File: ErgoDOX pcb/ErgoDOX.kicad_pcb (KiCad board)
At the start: 2 copper layers, 182.8 x 158.9 mm, 72 parts, among them J1 USB, J2 3.5mm, J3 JMP, J4 JMP, SW0:10 SW0:3, SW0:11 SW0:2, SW0:12 SW0:1, SW0:7 SW0:6, SW0:8 SW0:5, SW0:9 SW0:4, SW1:10 SW1:3, SW1:11 SW1:2, SW1:12 SW1:1, SW1:13 SW1:0, SW1:9 SW1:4, SW2:10 SW2:3, SW2:11 SW2:2, SW2:12 SW2:1, SW2:13 SW2:0, SW2:7 SW2:6, SW2:8 SW2:5, SW2:9 SW2:4, SW3:10 SW3:3, SW3:11 SW3:2, SW3:12 SW3:1, SW3:13 SW3:0, SW3:8 SW3:5, SW3:9 SW3:4, SW4:10 SW4:3, SW4:11 SW4:2, SW4:12 SW4:1, SW4:13 SW4:0, SW4:7 SW4:6, SW4:8 SW4:5, SW4:9 SW4:4, SW5:10 SW5:3, SW5:11 SW5:2, SW5:12 SW5:1, SW5:13 SW5:0, SW5:7 SW5:6, SW5:8 SW5:5, SW5:9 SW5:4, U1 TEENSY2.0, U2 MCP23018

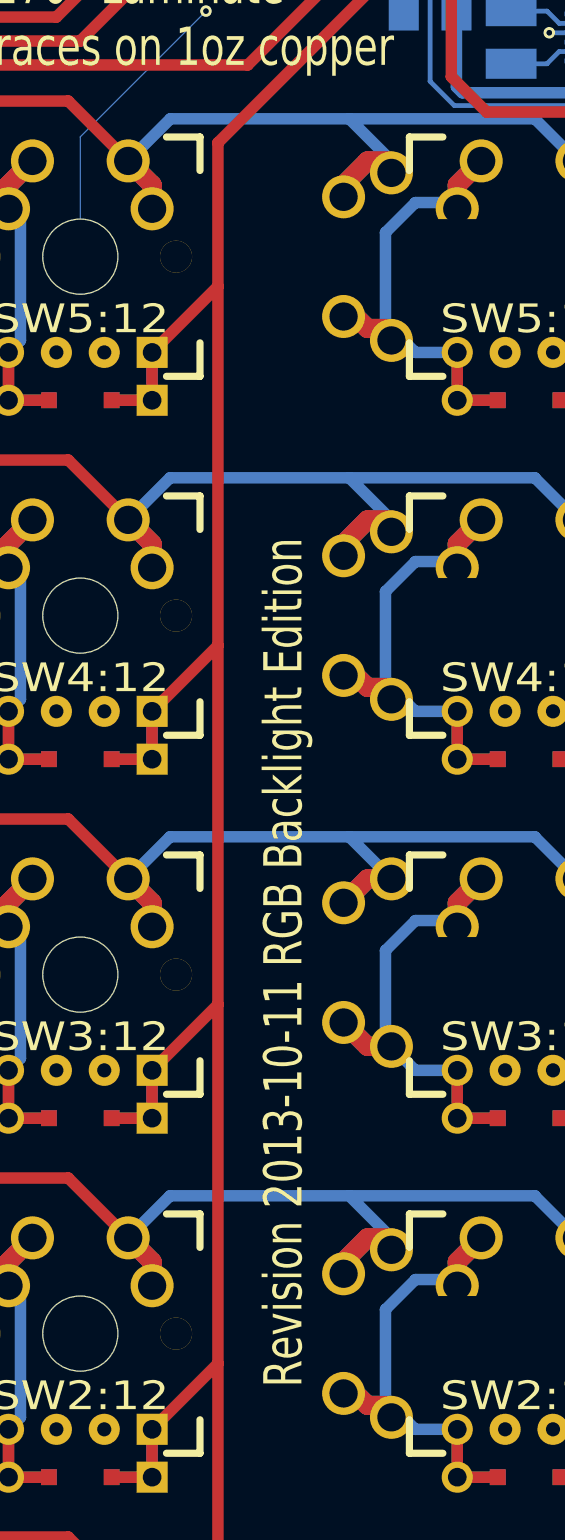
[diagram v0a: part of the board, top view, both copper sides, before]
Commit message: Fixed tracks around secondary outer most column
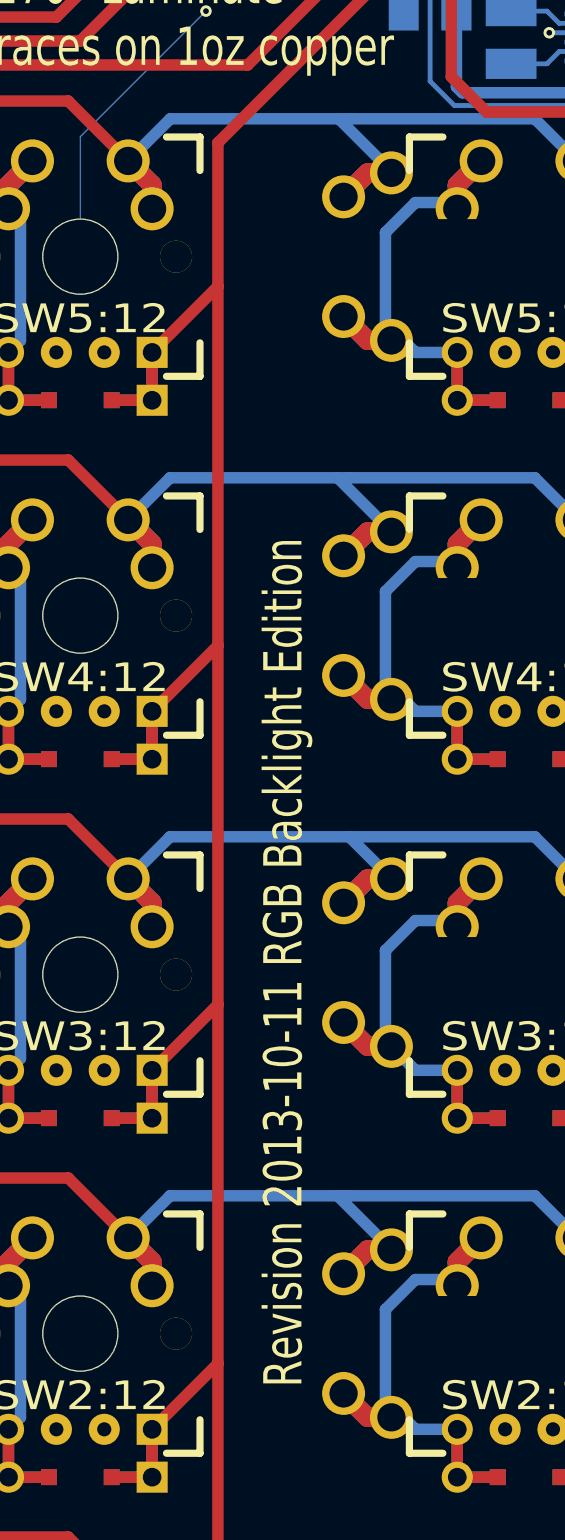
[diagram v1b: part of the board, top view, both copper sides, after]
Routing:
- net /ROW4: track 259.2 -> 260.1 mm
- net /ROW2: track 297.1 -> 298.0 mm
- net /ROW5: track 226.9 -> 227.7 mm

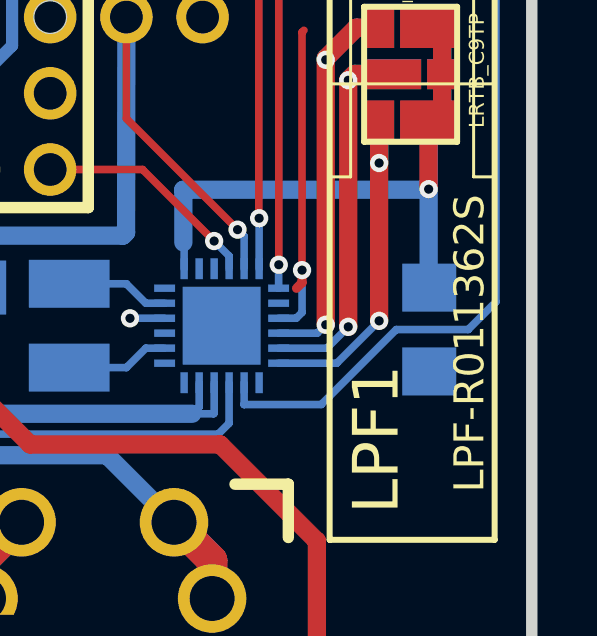
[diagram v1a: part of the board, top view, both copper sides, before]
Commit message: Allow output cap for led driver on either side.
Otherwise it might interfere with light tube.

Also fixed ground connection for all caps.
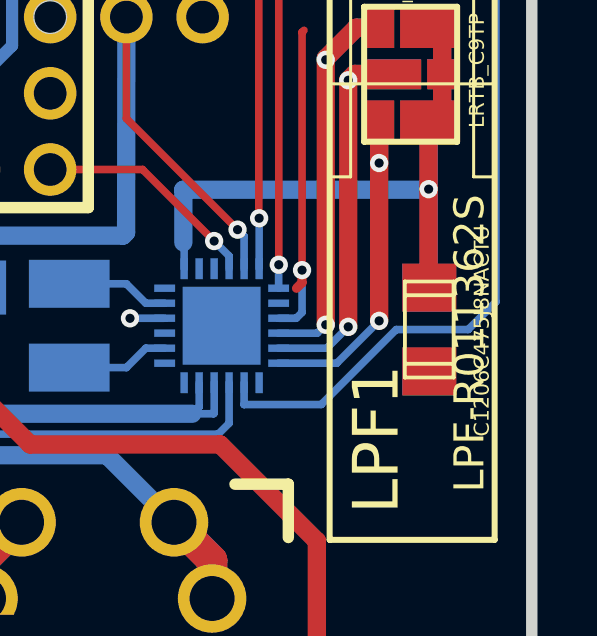
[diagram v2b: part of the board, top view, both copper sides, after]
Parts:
- added C1206C475J8NACTU: COUT1, C1206C475J8NACTU, F.Cu at (202.5, 55.5)
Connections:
- CIN1 pad 1: (no net) -> GND
- COUT1 pad 1: (no net) -> GND
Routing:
- net /V_OUT_C_CATHODE: track 25.8 -> 29.1 mm
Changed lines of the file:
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@@
 (kicad_pcb (version 3) (host pcbnew "(2013-07-07 BZR 4022)-stable")
   (general
-    (links 508)
-    (no_connects 3)
+    (links 511)
+    (no_connects 4)
     (area 22.890479 28.163519 259.962628 189.542421)
     (thickness 1.6002)
     (drawings 39)
-    (tracks 1306)
+    (tracks 1308)
     (zones 0)
-    (modules 72)
+    (modules 73)
     (nets 75)
   )
@@
     (mod_text_size 1.524 1.524)
     (mod_text_width 0.3048)
-    (pad_size 1.651 1.651)
-    (pad_drill 0.75)
+    (pad_size 1.6002 1.8034)
+    (pad_drill 0)
     (pad_to_mask_clearance 0.2032)
     (aux_axis_origin 0 0)
@@
     (pad 1 smd rect (at 1.397 0 180) (size 1.6002 1.8034)
       (layers Back B.Paste B.Mask)
+      (net 28 GND)
     )
     (pad 2 smd rect (at -1.397 0 180) (size 1.6002 1.8034)
@@
     (pad 1 smd rect (at 1.397 0 270) (size 1.6002 1.8034)
       (layers Back B.Paste B.Mask)
+      (net 28 GND)
     )
     (pad 2 smd rect (at -1.397 0 270) (size 1.6002 1.8034)
@@
     )
   )
+  (module C1206C475J8NACTU (layer Front)
+    (at 202.5015 55.499 270)
+    (descr "SMT capacitor, 1206")
+    (fp_text reference C1206C475J8NACTU (at 0.05 -1.75 270) (layer F.SilkS)
+      (effects (font (size 0.50038 0.50038) (thickness 0.11938)))
+    )
+    (fp_text value COUT1 (at 0.05 1.65 270) (layer F.SilkS) hide
+      (effects (font (size 0.50038 0.50038) (thickness 0.11938)))
+    )
+    (fp_line (start 1.143 0.8128) (end 1.143 -0.8128) (layer F.SilkS) (width 0.127))
+    (fp_line (start -1.143 -0.8128) (end -1.143 0.8128) (layer F.SilkS) (width 0.127))
+    (fp_line (start -1.6002 -0.8128) (end -1.6002 0.8128) (layer F.SilkS) (width 0.127))
+    (fp_line (start -1.6002 0.8128) (end 1.6002 0.8128) (layer F.SilkS) (width 0.127))
+    (fp_line (start 1.6002 0.8128) (end 1.6002 -0.8128) (layer F.SilkS) (width 0.127))
+    (fp_line (start 1.6002 -0.8128) (end -1.6002 -0.8128) (layer F.SilkS) (width 0.127))
+    (pad 1 smd rect (at 1.397 0 270) (size 1.6002 1.8034)
+      (layers Front F.Paste F.Mask)
+      (net 28 GND)
+    )
+    (pad 2 smd rect (at -1.397 0 270) (size 1.6002 1.8034)
+      (layers Front F.Paste F.Mask)
+    )
+    (model smd/capacitors/c_1206.wrl
+      (at (xyz 0 0 0))
+      (scale (xyz 1 1 1))
+      (rotate (xyz 0 0 0))
+    )
+  )
   (gr_text "Revision 2013-10-11 RGB Backlight Edition" (at 178.435 127 90) (layer F.SilkS)
     (effects (font (size 2.032 1.524) (thickness 0.3048)) (justify left))
@@
   (segment (start 171.45 139.39266) (end 171.45 140.66266) (width 1.016) (layer Back) (net 18))
   (segment (start 62.75832 145.59788) (end 64.9097 139.69238) (width 0.6096) (layer Back) (net 18))
-  (segment (start 184.15 119.70766) (end 184.15 119.6975) (width 0.6096) (layer Back) (net 19) (status C00000))
-  (segment (start 184.15 119.6975) (end 181.2925 116.84) (width 0.6096) (layer Back) (net 19) (status 400000))
+  (segment (start 184.15 119.70766) (end 184.15 119.6975) (width 0.6096) (layer Back) (net 19))
+  (segment (start 184.15 119.6975) (end 181.2925 116.84) (width 0.6096) (layer Back) (net 19))
   (segment (start 184.15 119.70766) (end 182.88 119.70766) (width 1.016) (layer Back) (net 19))
   (segment (start 182.88 119.70766) (end 181.61 120.97766) (width 1.016) (layer Back) (net 19))
@@
   (segment (start 188.595 46.0375) (end 186.3725 48.26) (width 0.4064) (layer Back) (net 26))
   (segment (start 176.2125 46.6725) (end 160.9725 46.6725) (width 0.4064) (layer Front) (net 26))
+  (segment (start 202.48 50.82) (end 202.48 54.0805) (width 0.6096) (layer Front) (net 27) (status 800000))
+  (segment (start 202.48 54.0805) (end 202.5015 54.102) (width 0.6096) (layer Front) (net 27) (status C00000))
   (segment (start 202.48 50.82) (end 202.48 54.083) (width 0.6096) (layer Back) (net 27))
   (segment (start 194.303 50.84) (end 202.46 50.84) (width 0.6096) (layer Back) (net 27))

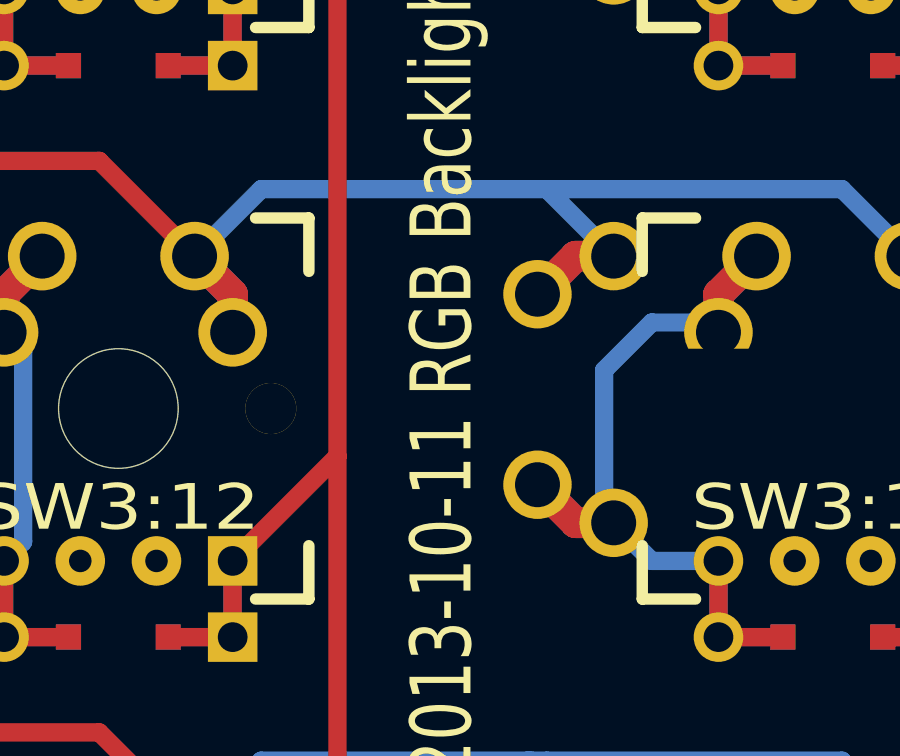
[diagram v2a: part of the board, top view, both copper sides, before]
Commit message: Fixed last switch secondary switch pos.
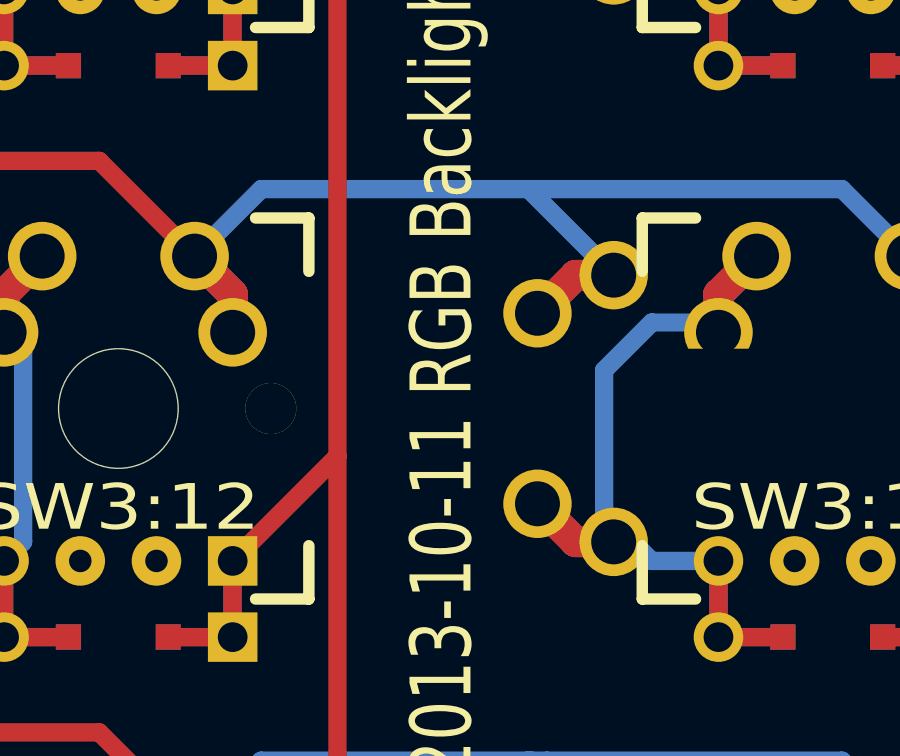
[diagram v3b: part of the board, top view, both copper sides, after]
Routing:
- net /ROW3: track 240.5 -> 241.4 mm

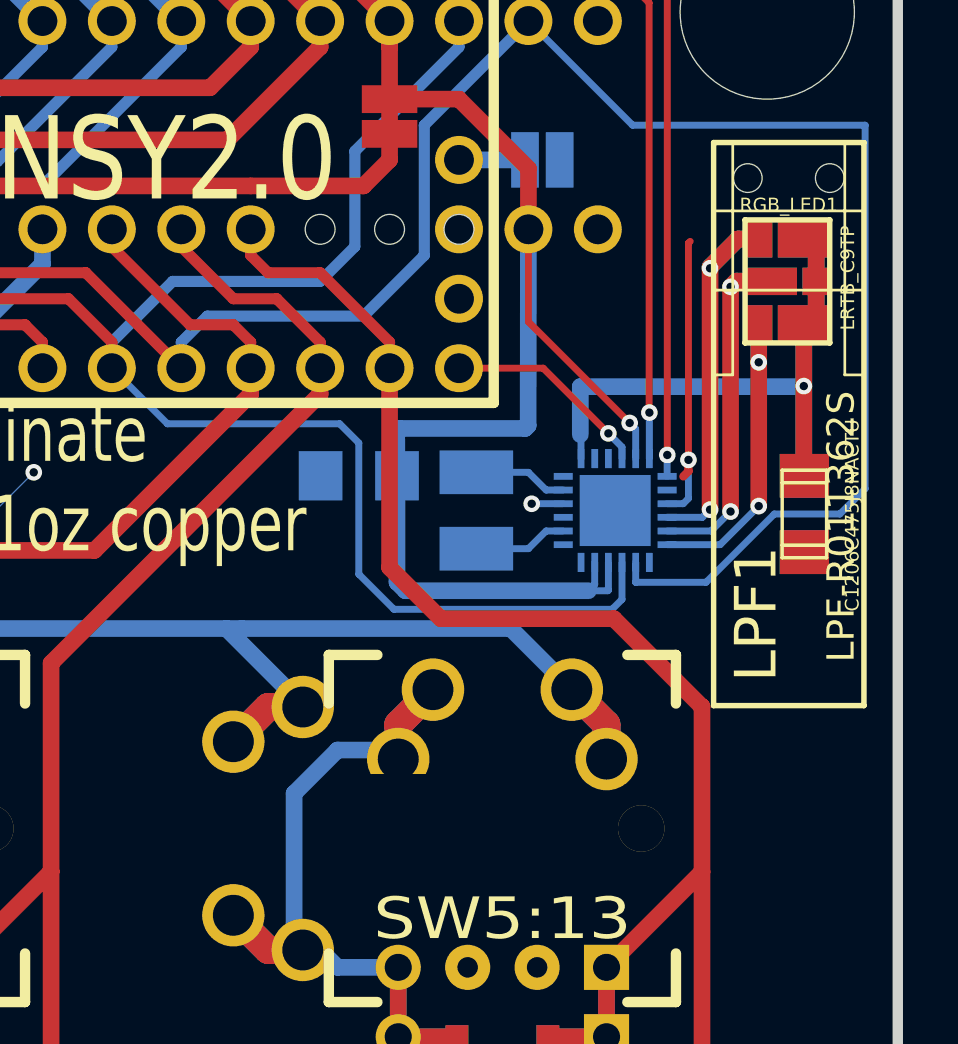
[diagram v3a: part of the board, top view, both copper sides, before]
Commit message: Allow dual side caps and inductor
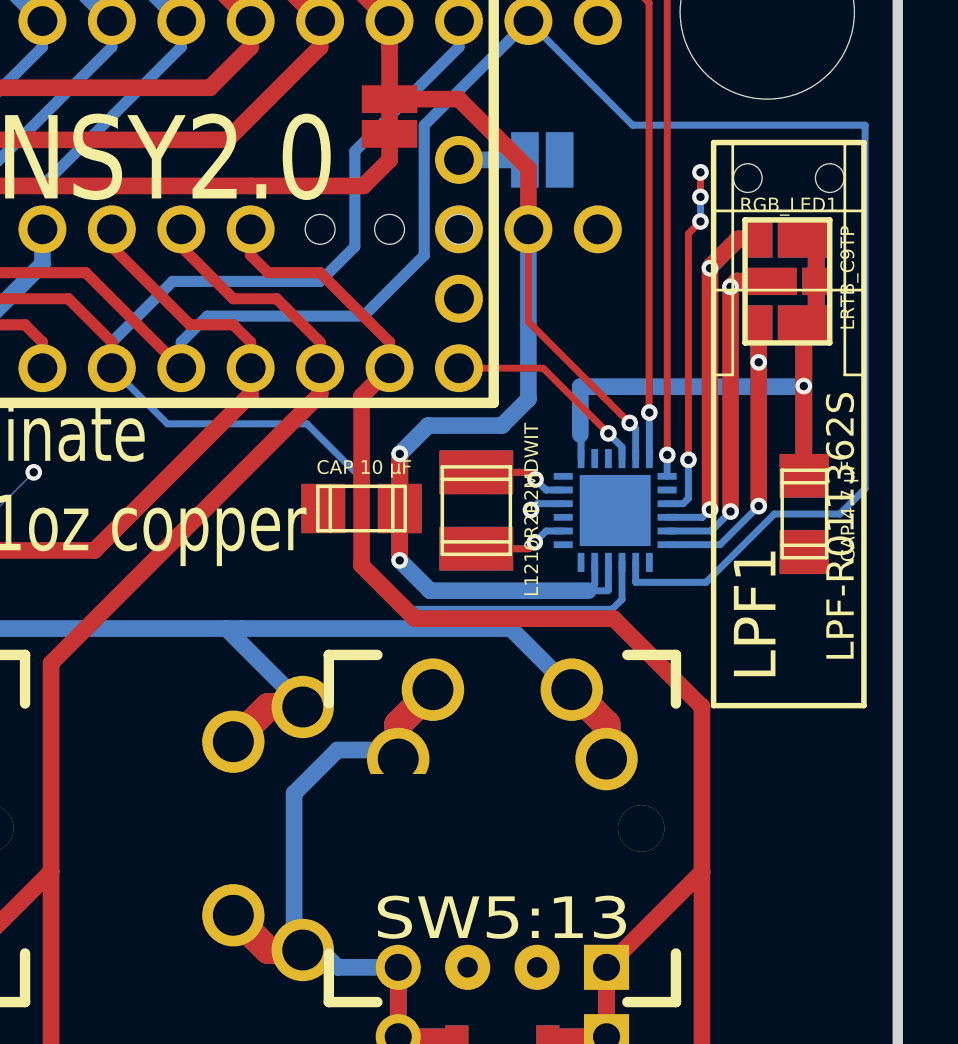
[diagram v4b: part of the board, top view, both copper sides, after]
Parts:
- added CAP 10 µF: CIN1, C1206C106J8RACTU, F.Cu at (186.3, 55.3)
- added L1210R2R2MDWIT: L1, L1210R2R2MDWIT, F.Cu at (190.5, 55.4)
- CAP 4.7 µF: renamed from C1206C475J8NACTU
- COUT1: value CAP 4.7 µF, 6.3V/10V X7R -> CAP 4.7 µF
- moved CIN1 1.20 mm to (186.3, 55.3)
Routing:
- net /L2_T1: track 3.45 -> 5.72 mm, vias 0 -> 1
- net /L1_T1: track 3.45 -> 5.68 mm, vias 0 -> 1
- net VCC: track 198.1 -> 200.2 mm, vias 1 -> 3
- net GND: track 118.0 -> 120.1 mm, vias 8 -> 11
- net /COL0: track 163.4 -> 164.8 mm
- net /SCLM: track 146.5 -> 145.5 mm
